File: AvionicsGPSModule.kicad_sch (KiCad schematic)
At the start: 54 parts, among them P1 MC311D, Q1 AO3400A, Q2 AO3400A, U1 RP2040, U2 AP2112K-3.3, U3 L80-R, U4 W25Q128JVS, U5 SN65HVD230DR, U6 MCP2515_I/ML, X1 ABM8-272-T3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

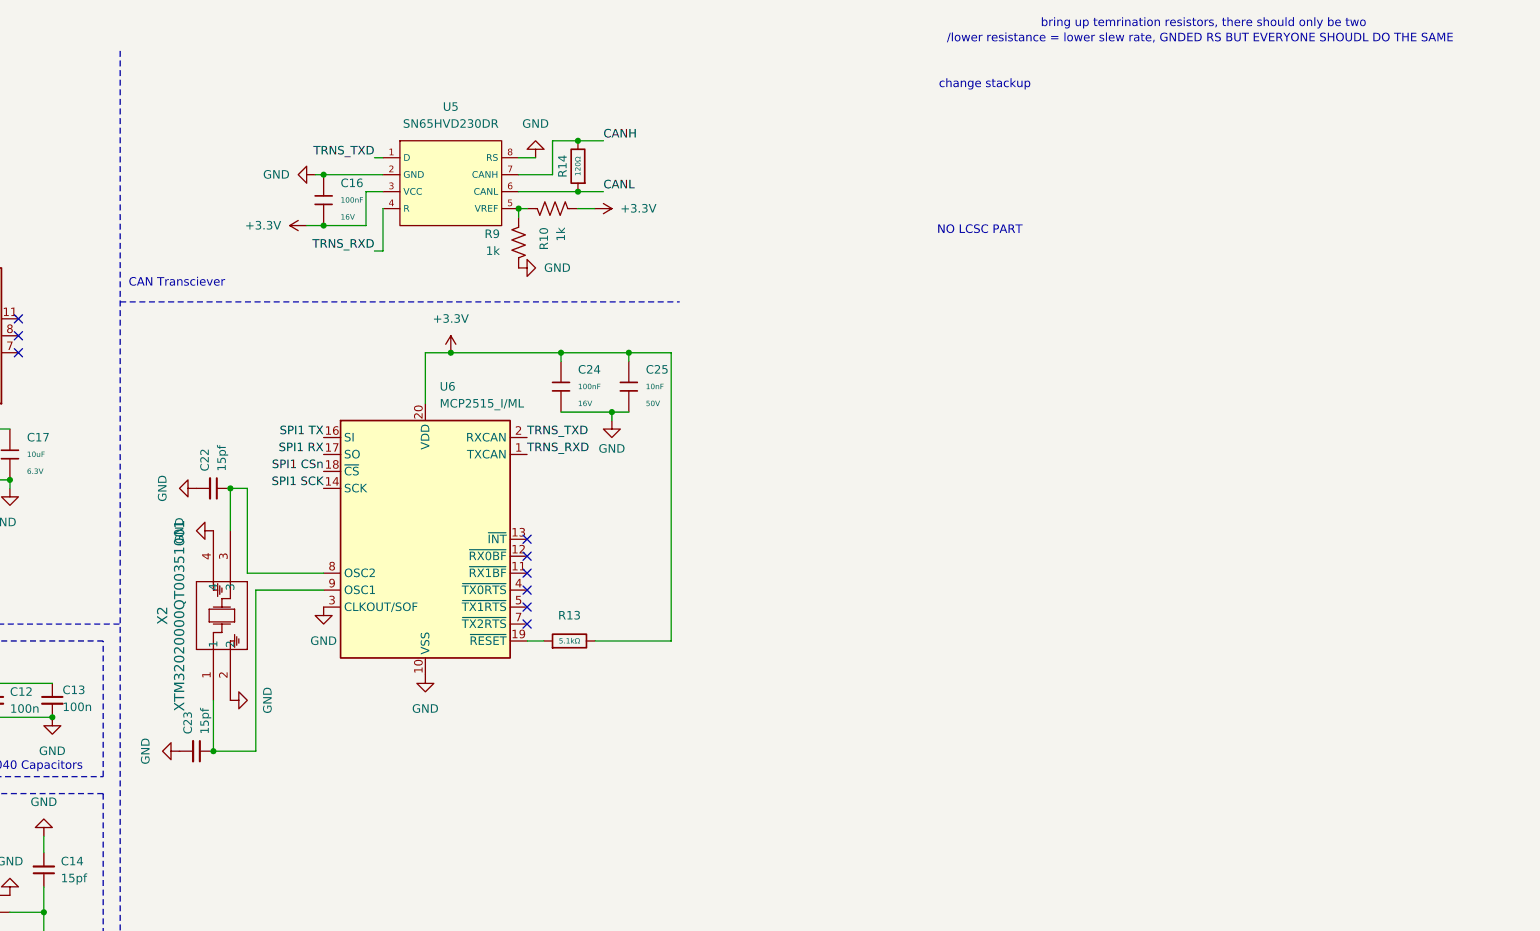
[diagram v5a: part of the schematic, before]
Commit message: Updated BOM, made schematic cleaner
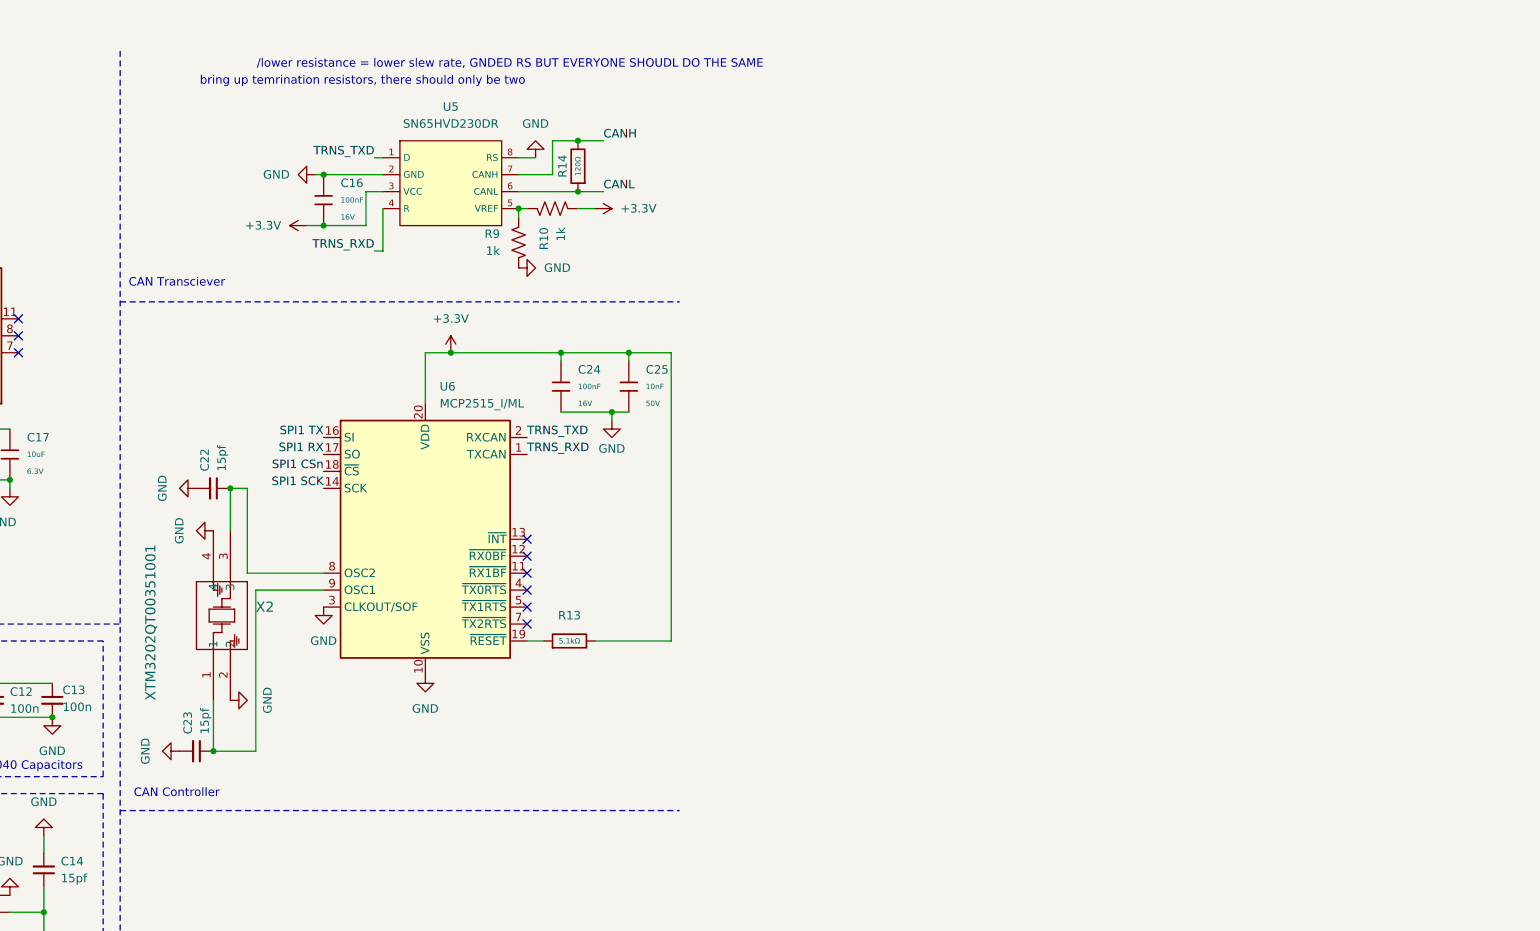
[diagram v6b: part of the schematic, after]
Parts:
- U6: LCSC (none) -> C96140
- X2: value XTM32020000QT00351001 -> XTM3202QT00351001
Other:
- note added: "CAN Controller"
- note removed: "NO LCSC PART"
- note removed: "change stackup"
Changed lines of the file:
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@@
 		)
 	)
+	(text "CAN Controller\n"
+		(exclude_from_sim no)
+		(at 202.692 125.222 0)
+		(effects
+			(font
+				(size 1.27 1.27)
+			)
+			(justify left bottom)
+		)
+	)
 	(text "RP2040 Capacitors\n"
 		(exclude_from_sim no)
@@
 	(text "/lower resistance = lower slew rate, GNDED RS BUT EVERYONE SHOUDL DO THE SAME\n\n"
 		(exclude_from_sim no)
-		(at 362.458 12.446 0)
-		(effects
-			(font
-				(size 1.27 1.27)
-			)
-		)
-	)
-	(text "change stackup\n"
-		(exclude_from_sim no)
-		(at 330.2 18.288 0)
-		(effects
-			(font
-				(size 1.27 1.27)
-			)
-		)
-	)
-	(text "NO LCSC PART"
-		(exclude_from_sim no)
-		(at 329.438 40.132 0)
+		(at 259.08 16.256 0)
 		(effects
 			(font
@@
 	(text "bring up temrination resistors, there should only be two\n"
 		(exclude_from_sim no)
-		(at 362.966 9.144 0)
+		(at 236.982 17.78 0)
 		(effects
 			(font
@@
 		)
 	)
+	(polyline
+		(pts
+			(xy 200.66 127) (xy 284.48 127)
+		)
+		(stroke
+			(width 0)
+			(type dash)
+		)
+	)
 	(wire
 		(pts
@@
 			)
 		)
-		(property "LCSC" ""
+		(property "LCSC" "C96140"
 			(at 246.38 86.36 0)
 			(effects
@@
 		(on_board yes)
 		(dnp no)
-		(fields_autoplaced yes)
 		(property "Reference" "X2"
-			(at 207.01 97.79 0)
+			(at 220.98 96.5199 90)
 			(effects
 				(font
 					(size 1.524 1.524)
 				)
+				(justify right)
 			)
 		)
-		(property "Value" "XTM32020000QT00351001"
-			(at 209.55 97.79 0)
+		(property "Value" "XTM3202QT00351001"
+			(at 205.232 87.122 0)
 			(effects
 				(font
 					(size 1.524 1.524)
 				)
+				(justify right)
 			)
 		)

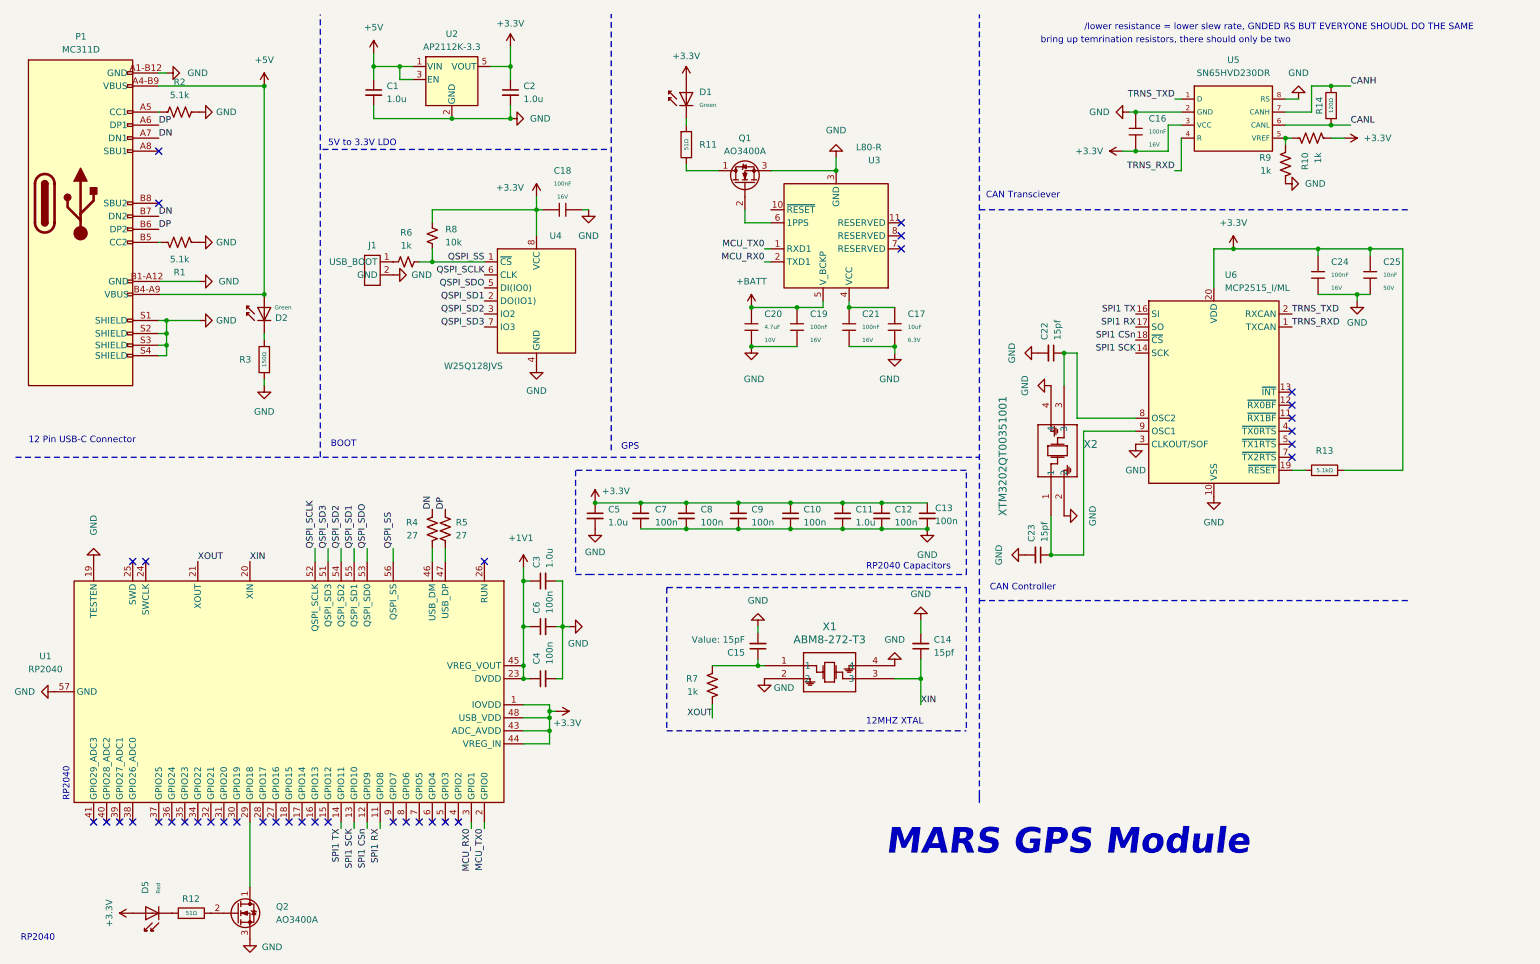
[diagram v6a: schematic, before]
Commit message: Respecced crystal, added Schottky Diode
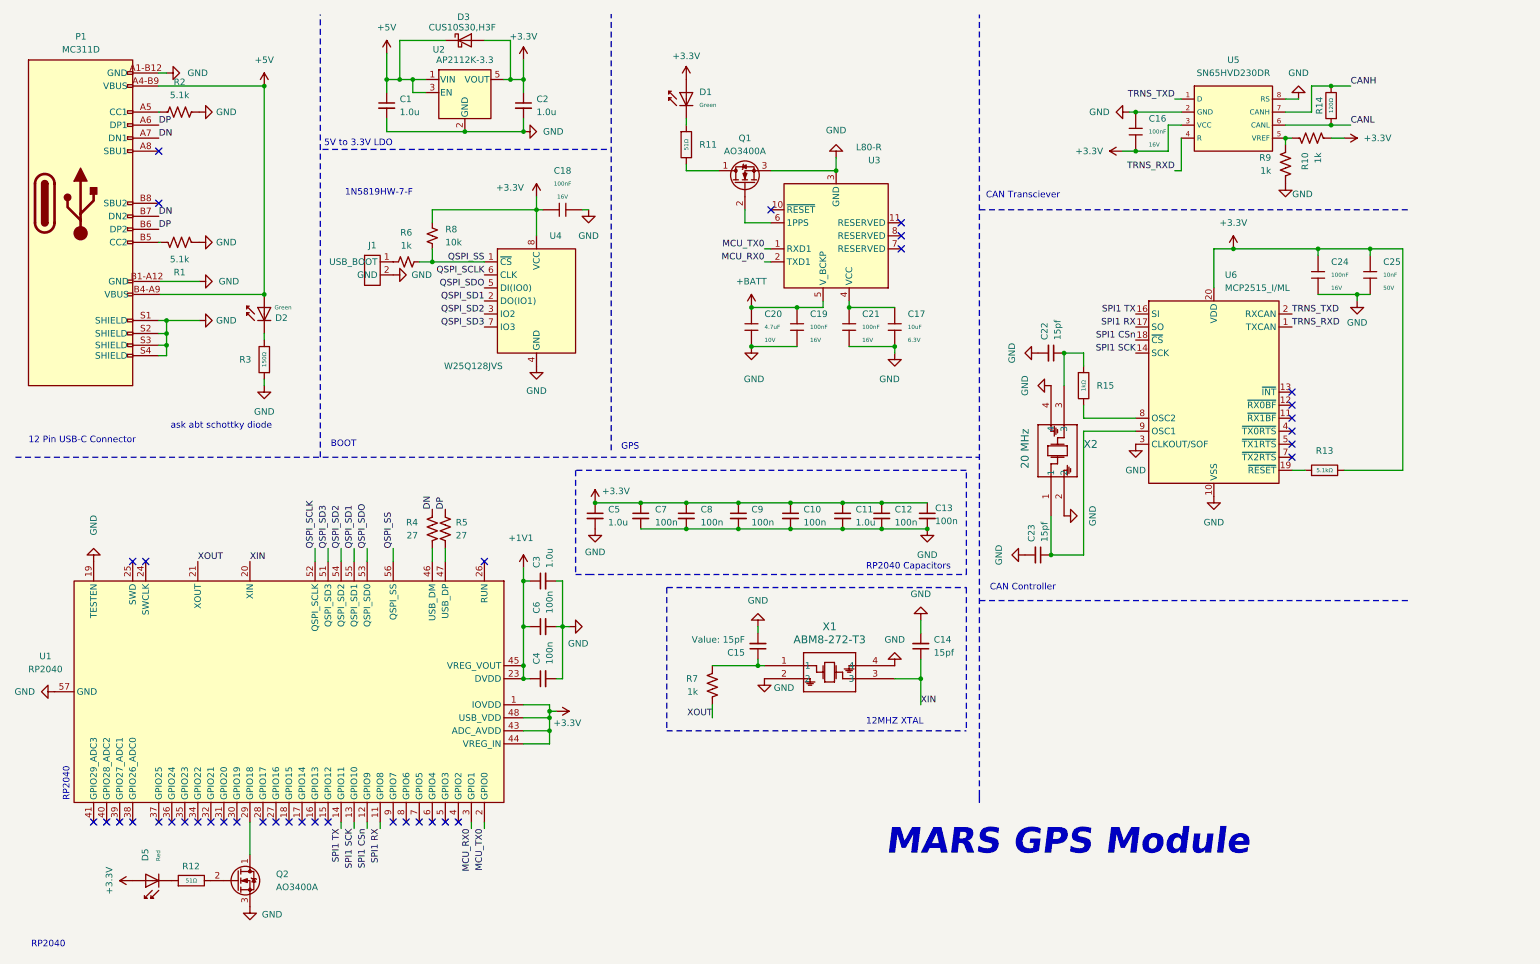
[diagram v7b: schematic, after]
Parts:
- added D3: CUS10S30,H3F, Diode_SMD:D_SOD-323, symbol Diode:1N5819
- added R15: 1kΩ, PCM_JLCPCB:R_0402, symbol PCM_JLCPCB-Resistors:0402,1kΩ
- X2: value XTM3202QT00351001 -> 20 MHz; footprint Crystal:Crystal_SMD_3225-4Pin_3.2x2.5mm -> Crystal:Crystal_SMD_2016-4Pin_2.0x1.6mm; LCSC C37635374 -> C255878
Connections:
- net +3.3V: now also D3.2 (A)
- net +5V: now also D3.1 (K)
- net at C22.1, X2.3: now also R15.1; no longer U6.8 (OSC2)
- new net: R15.2, U6.8 (OSC2)
- no-connect marks 37 -> 38
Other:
- note added: "1N5819HW‑7‑F"
- note added: "ask abt schottky diode"
- note removed: "/lower resistance = lower slew rate, GNDED RS BUT EVERYONE SHOUDL DO THE SAME"
- note removed: "bring up temrination resistors, there should only be two"
- moved on the sheet: C1, C2, D5, Q2, R12, U2

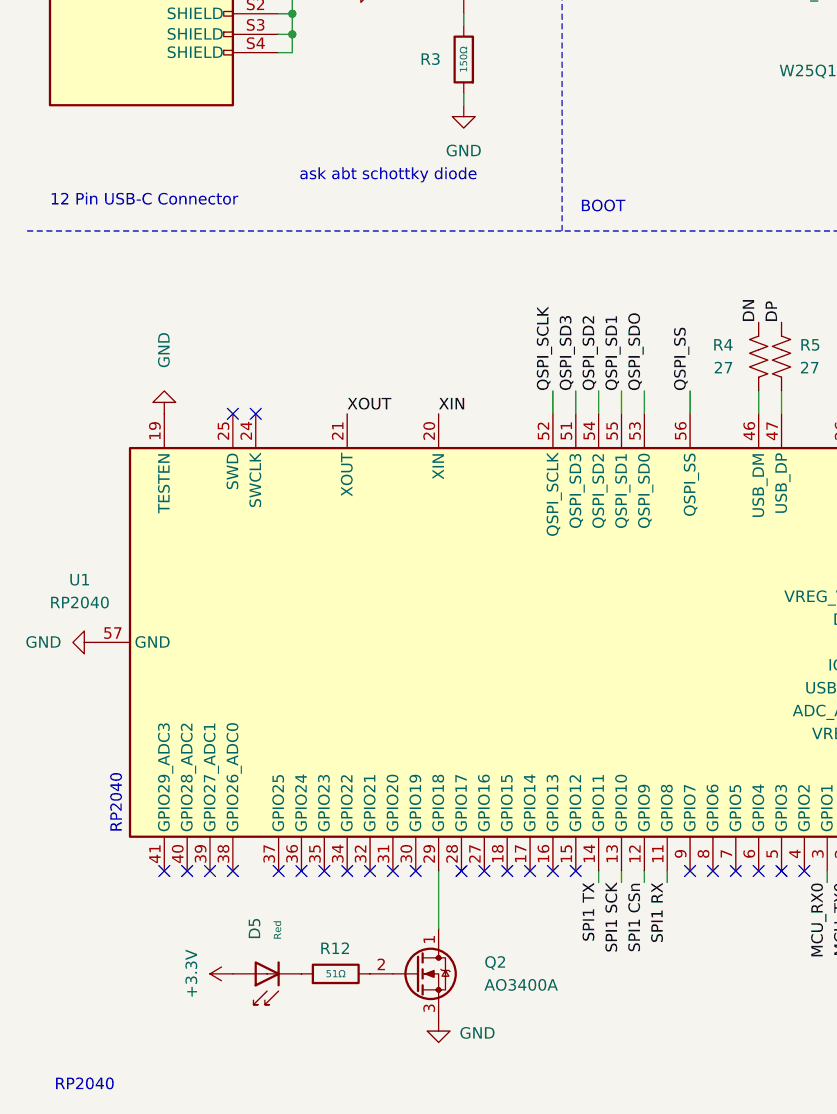
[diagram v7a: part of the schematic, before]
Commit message: Fixed MOSFET Driver
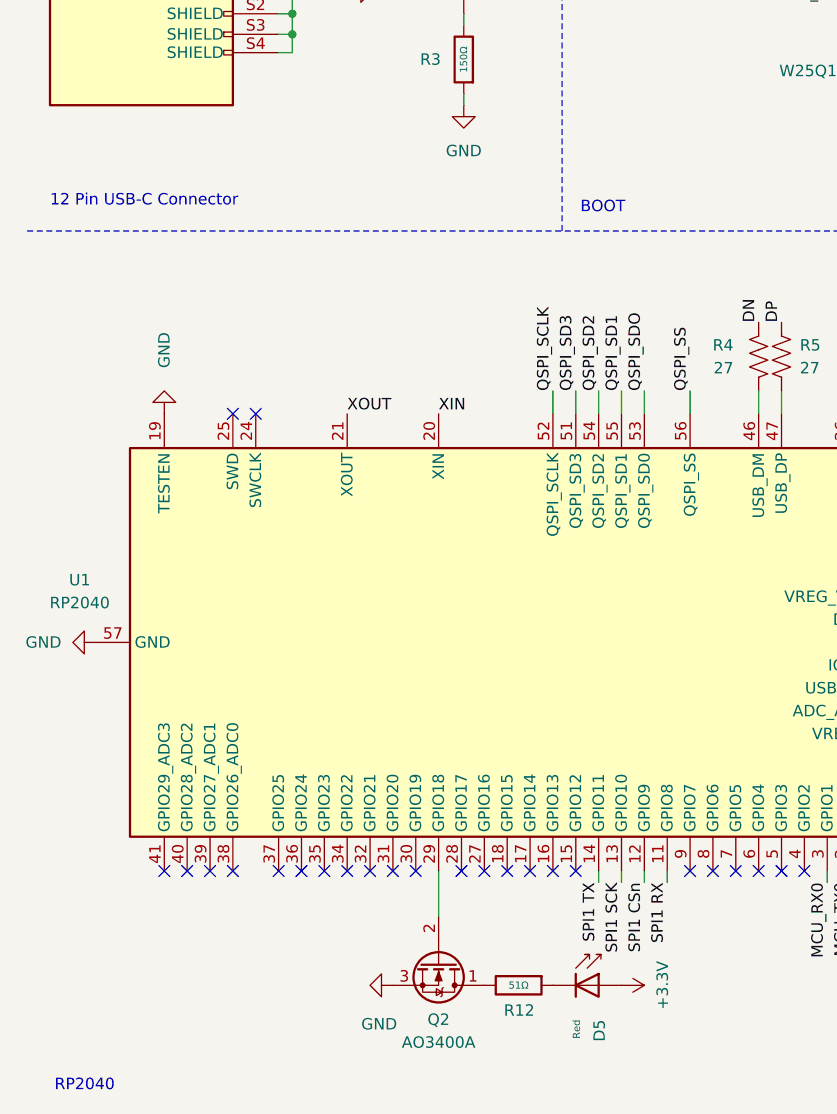
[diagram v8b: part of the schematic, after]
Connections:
- net at Q2.1 (D): now also R12.2; no longer U1.29 (GPIO18)
- net at Q2.2 (G): now also U1.29 (GPIO18); no longer R12.2
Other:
- note removed: "ask abt schottky diode"
- moved on the sheet: D5, Q2, R12
